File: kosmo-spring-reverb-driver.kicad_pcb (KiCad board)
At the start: 2 copper layers, 50 x 200 mm, 48 parts, among them Q1 BC639, Q2 BC640, U1 TL074

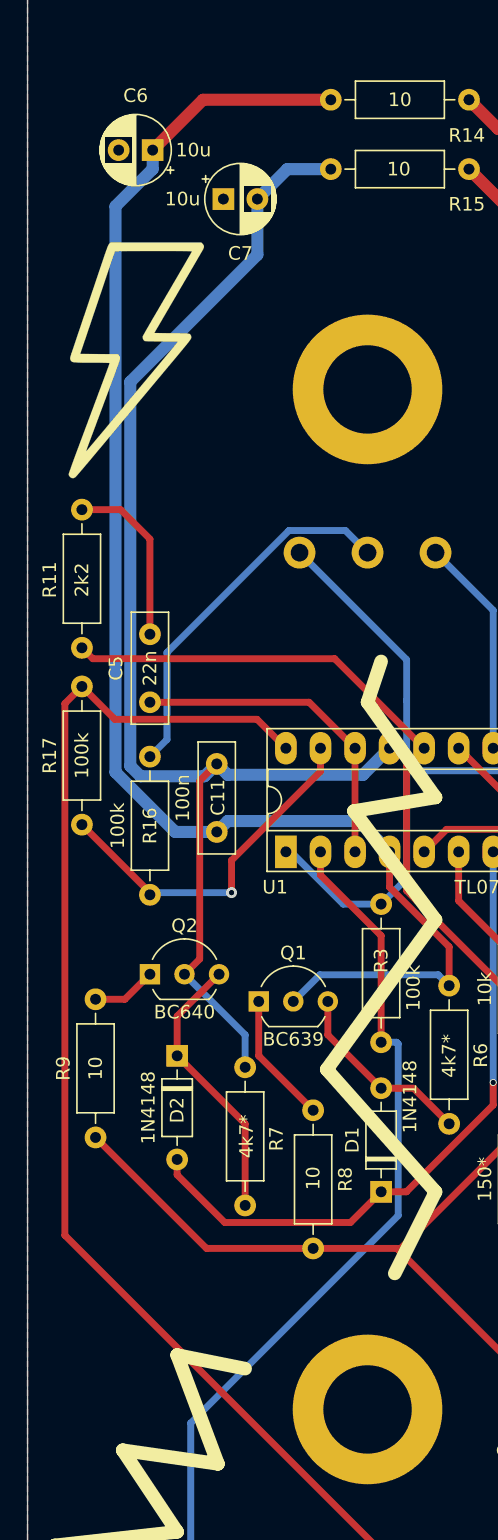
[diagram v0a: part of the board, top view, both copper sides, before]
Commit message: Fix pot hole size, cap position
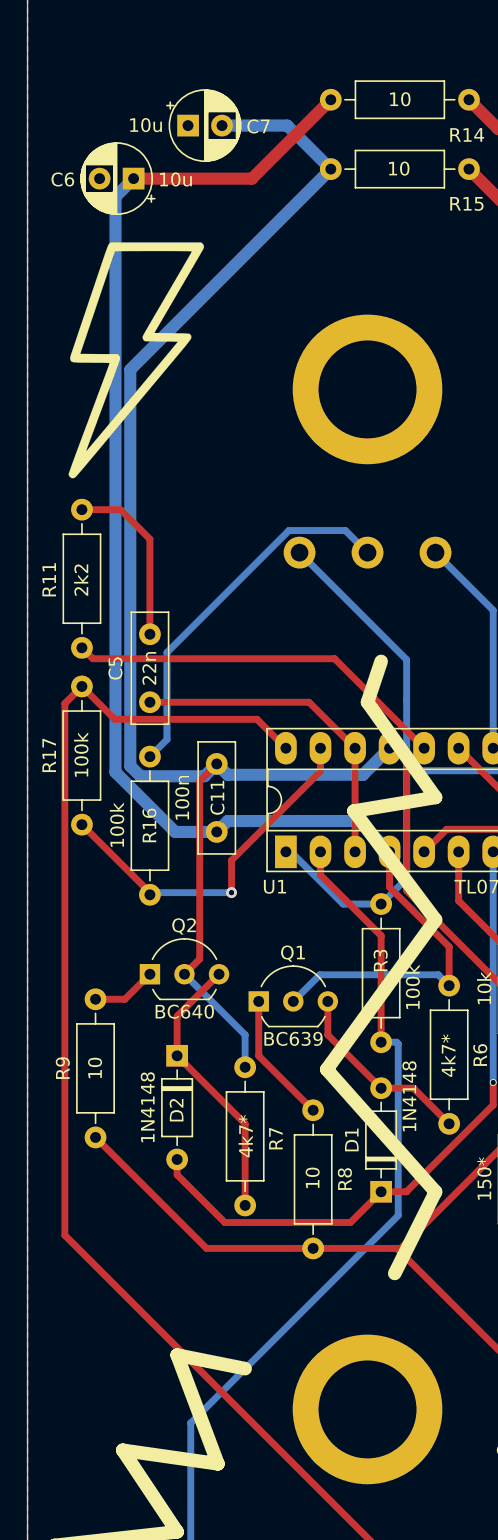
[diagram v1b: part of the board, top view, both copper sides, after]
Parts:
- moved C7 5.99 mm to (93.8, 71.6)
- moved C6 2.52 mm to (89.8, 75.5)
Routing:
- net -12V: track 97.9 -> 105.4 mm
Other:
- board text added: "Kosmo Spring Reverb Driver v1.0.1 Jan Knipper 2021 github.com/polykit"
- board text removed: "Kosmo Spring Reverb Driver v1.0.0 Jan Knipper 2021 github.com/polykit"

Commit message: Redo gerber files
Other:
- net class Default removed
